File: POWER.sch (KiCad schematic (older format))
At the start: 0 parts

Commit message: Started PCB Layout, added mounting holes, connectors, in correct locations
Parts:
- added C36, C37, C40, C41: 10uF, Capacitors_SMD:C_0805, symbol C
- added C38, C39: 4.7uF, Capacitors_SMD:C_0805, symbol C
- added D4: LED, Capacitors_SMD:C_0603, symbol LED
- added J3: RAPC712x, symbol RAPC712x
- added L1, L2: 2.2uH, Capacitors_SMD:C_1206, symbol L
- added R27: 200, Resistors_SMD:R_0805, symbol R
- added R28: 270, Resistors_SMD:R_0603, symbol R
- added R29, R30: 150k, Resistors_SMD:R_0603, symbol R
- added R32: 300k, Resistors_SMD:R_0603, symbol R
- added R33: 680k, Resistors_SMD:R_0603, symbol R
- added U10, U11: TPS62260, symbol TPS62260
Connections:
- new net: D4.1 (A), R28.1
- new net: L1.1, U10.1 (SW)
- new net: R29.1, R32.2, U10.3 (FB)
- new net: L2.1, U11.1 (SW)
- new net: R30.1, R33.2, U11.3 (FB)
- new net +1V8: C40.1, L1.2, R32.1
- new net +3V3: C41.1, L2.2, R33.1
- new net GND: C36.2, C37.2, C38.2, C39.2, C40.2, C41.2, D4.2 (K), J3.2, J3.3, R27.2, R29.2, R30.2, U10.6 (GND), U10.7 (PP), U11.6 (GND), U11.7 (PP)
- new net SYSPWR: C36.1, C37.1, C38.1, C39.1, J3.1, R27.1, R28.2, U10.2 (MODE), U10.4 (EN), U10.5 (VIN), U11.2 (MODE), U11.4 (EN), U11.5 (VIN)

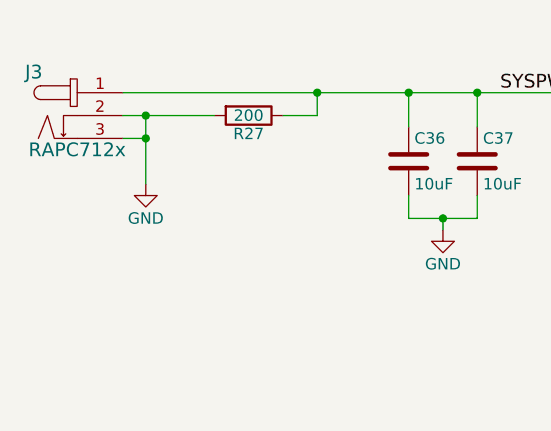
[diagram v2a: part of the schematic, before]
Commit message: Basic layout of all components on PCB
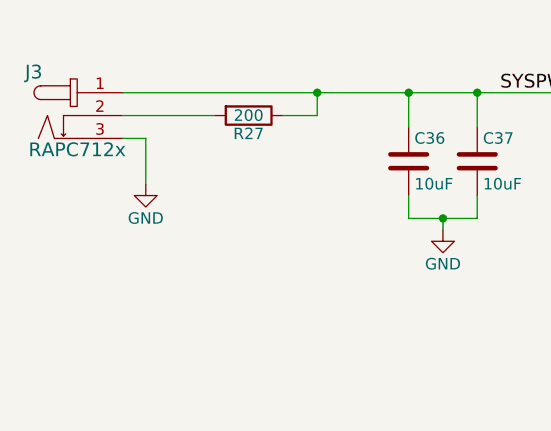
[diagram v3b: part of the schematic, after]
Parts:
- J3: footprint (none) -> misc:RAPC712
- U10, U11: footprint (none) -> misc:WSON-6
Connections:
- net GND: no longer J3.2, R27.2
- new net: J3.2, R27.2
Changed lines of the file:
@@
 F 0 "J3" H 1810 2890 60  0000 C CNN
 F 1 "RAPC712x" H 2000 2550 60  0000 C CNN
-F 2 "" H 1950 2650 60  0001 C CNN
+F 2 "misc:RAPC712" H 1950 2650 60  0001 C CNN
 F 3 "" H 1950 2650 60  0000 C CNN
 F 4 "RAPC712X" H 1900 3000 60  0001 C CNN "Part #"
@@
 	2200 2600 2600 2600
 Wire Wire Line
-	2300 2600 2300 2900
-Wire Wire Line
 	2300 2700 2200 2700
-Connection ~ 2300 2600
-Connection ~ 2300 2700
 Wire Wire Line
 	2200 2500 4600 2500
@@
 F 0 "U10" H 6700 3200 60  0000 C CNN
 F 1 "TPS62260" H 6950 2650 60  0000 C CNN
-F 2 "" V 7300 2900 60  0001 C CNN
+F 2 "misc:WSON-6" V 7300 2900 60  0001 C CNN
 F 3 "" V 7300 2900 60  0000 C CNN
 F 4 "TPS62260DRVT" H 7100 3150 60  0001 C CNN "Part #"
@@
 F 0 "U11" H 6700 4500 60  0000 C CNN
 F 1 "TPS62260" H 6950 3950 60  0000 C CNN
-F 2 "" V 7300 4200 60  0001 C CNN
+F 2 "misc:WSON-6" V 7300 4200 60  0001 C CNN
 F 3 "" V 7300 4200 60  0000 C CNN
 F 4 "TPS62260DRVT" H 7100 4450 60  0001 C CNN "Part #"
@@
 Wire Wire Line
 	9400 4600 9400 4450
+Wire Wire Line
+	2300 2900 2300 2700
 $EndSCHEMATC

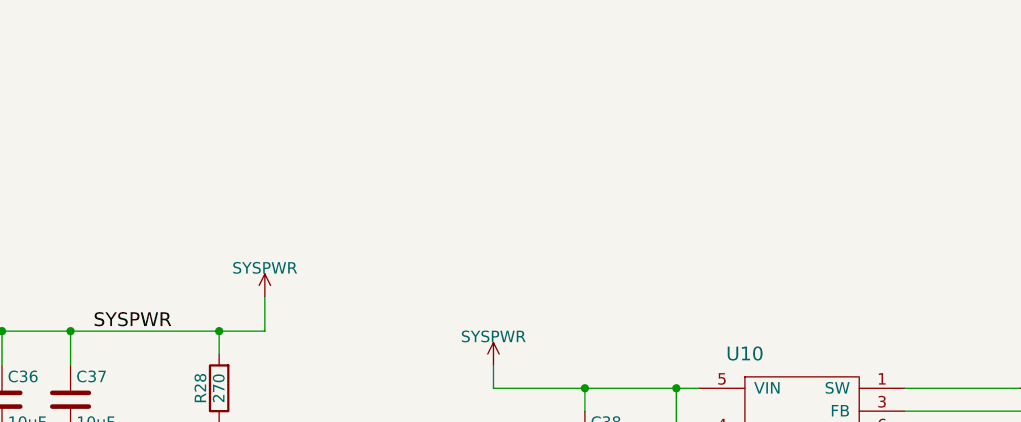
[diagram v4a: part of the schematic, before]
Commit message: Schematic Titles
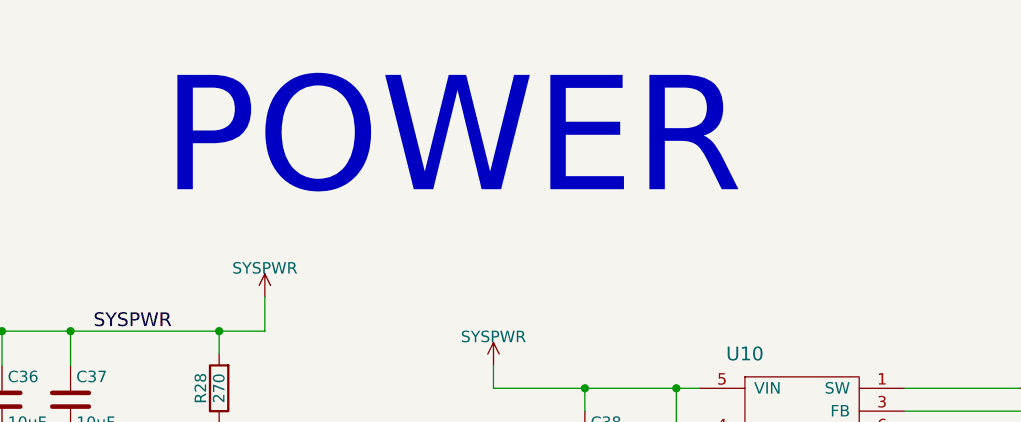
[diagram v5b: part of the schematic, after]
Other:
- note added: "POWER"
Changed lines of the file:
@@
 Wire Wire Line
 	2300 2900 2300 2700
+Text Notes 4150 1950 0    500  ~ 0
+POWER
 $EndSCHEMATC
